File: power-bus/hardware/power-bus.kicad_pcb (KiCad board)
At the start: 2 copper layers, 68.6 x 109.2 mm, 18 parts, among them J1 CONN_01X02, J10 CONN_01X02, J11 CONN_01X02, J12 CONN_01X02, J13 CONN_01X02, J2 CONN_01X02, J3 CONN_01X02, J4 CONN_01X02, J5 CONN_01X02, J6 CONN_01X02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

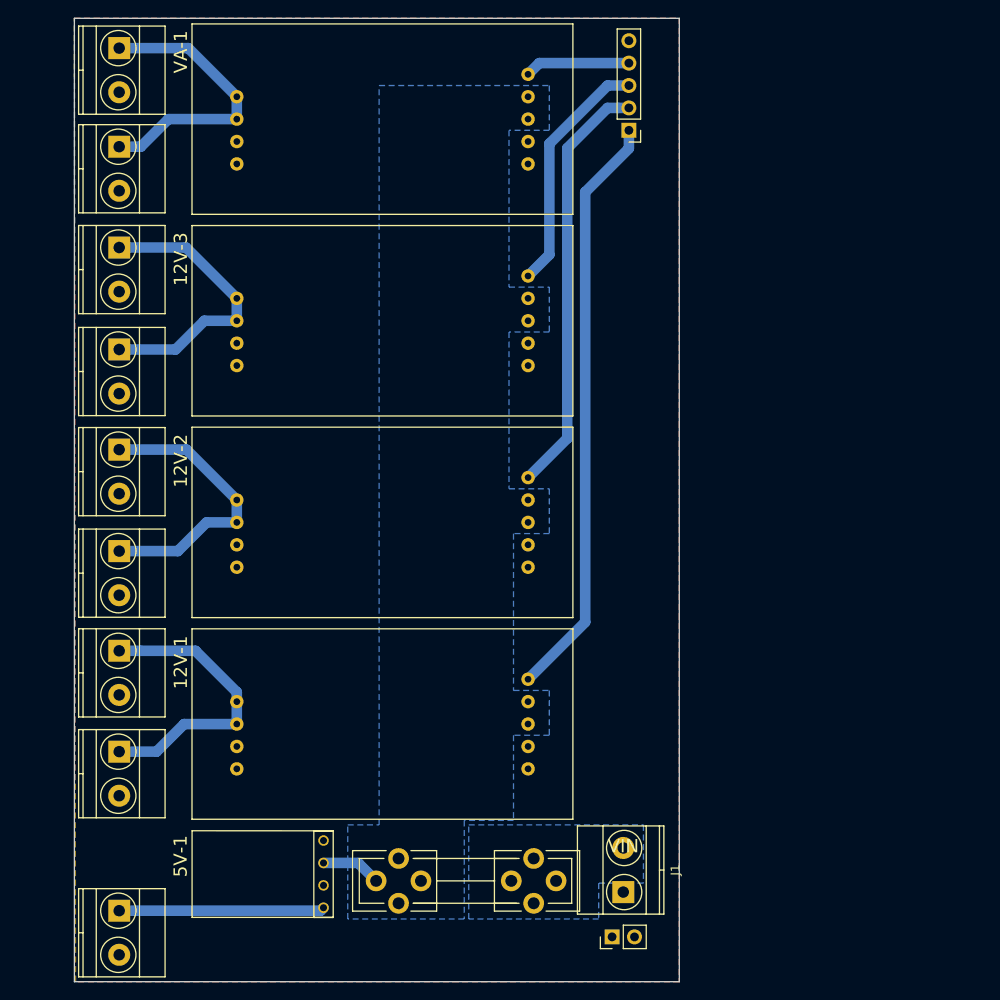
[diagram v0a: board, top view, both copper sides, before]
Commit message: Rotate 90 degrees.
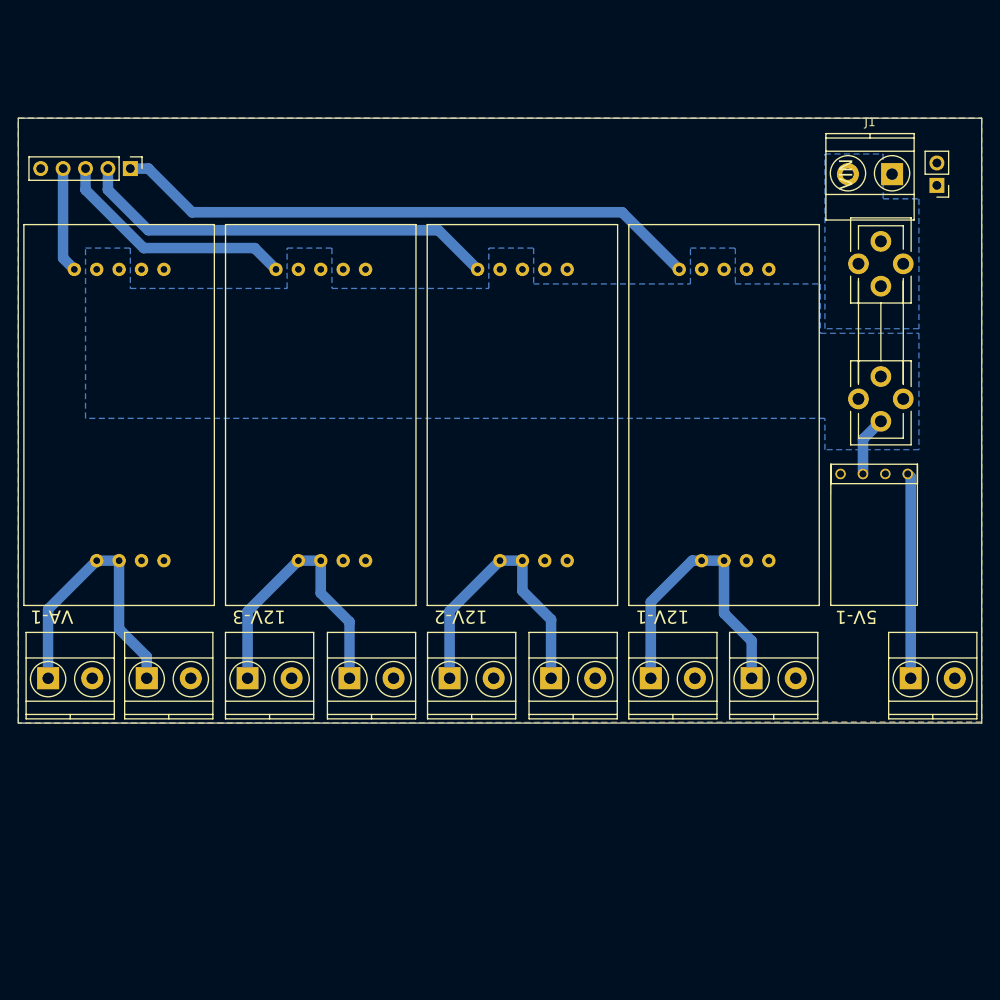
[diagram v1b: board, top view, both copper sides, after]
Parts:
- moved J2 93.5 mm to (183.7, 112.9), turned to 0 degrees
- moved J13 92.8 mm to (186.7, 57.0), turned to 180 degrees
- moved J1 86.9 mm to (181.6, 55.8), turned to 180 degrees
- moved F1 77.4 mm to (180.3, 83.8), turned to 90 degrees
- moved U1 77.2 mm to (179.6, 89.8), turned to 180 degrees
- moved J7 72.2 mm to (165.7, 112.9), turned to 0 degrees
- moved J12 71.9 mm to (85.9, 112.9), turned to 0 degrees
- moved J3 60.4 mm to (154.3, 112.9), turned to 0 degrees
- moved J6 60.3 mm to (97.1, 112.9), turned to 0 degrees
- moved J9 56.7 mm to (95.2, 55.1), turned to 270 degrees
- moved U2 54.0 mm to (163.8, 81.8), turned to 90 degrees
- moved J4 51.0 mm to (142.9, 112.9), turned to 0 degrees
- moved J11 51.0 mm to (108.5, 112.9), turned to 0 degrees
- moved J10 45.6 mm to (131.4, 112.9), turned to 0 degrees
- moved J5 45.5 mm to (120.1, 112.9), turned to 0 degrees
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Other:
- board size 68.6 x 109.2 mm -> 109.2 x 68.6 mm
